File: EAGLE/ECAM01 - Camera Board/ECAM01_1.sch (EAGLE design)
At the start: 51 parts, among them J1 DCMI-PRELIM, J2 I2C1-2, J3 CPL-ETH-MAGJACK-PULSE, J4 USART1, J5 USART2, J6 CPL-CON-USB-B, Q1 TBD, Q2 25MHz, U1 32F429ZIT6U, U2 IS45S16400J, U3 CPL-ETH-PHY-LAN8720A, U4 74LVC1G04

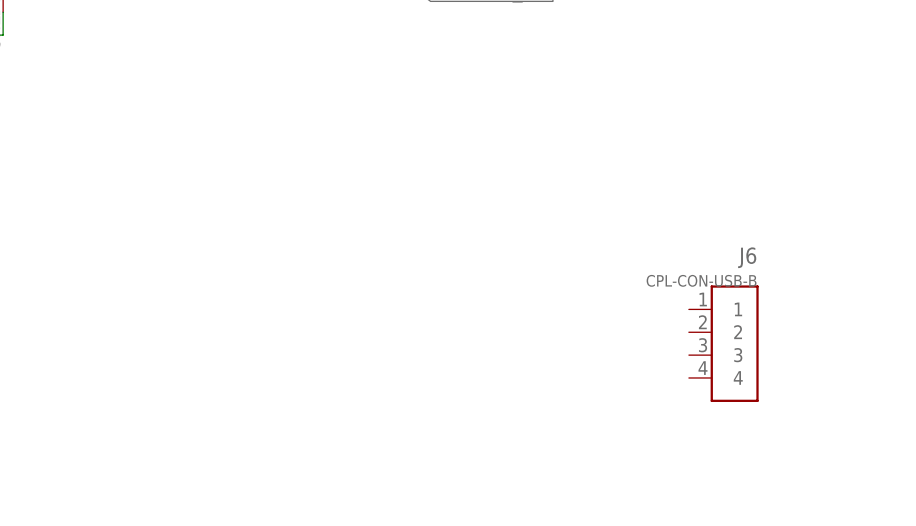
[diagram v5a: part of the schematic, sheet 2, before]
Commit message: Added USB connection to ECAM01 board, relevant devices.
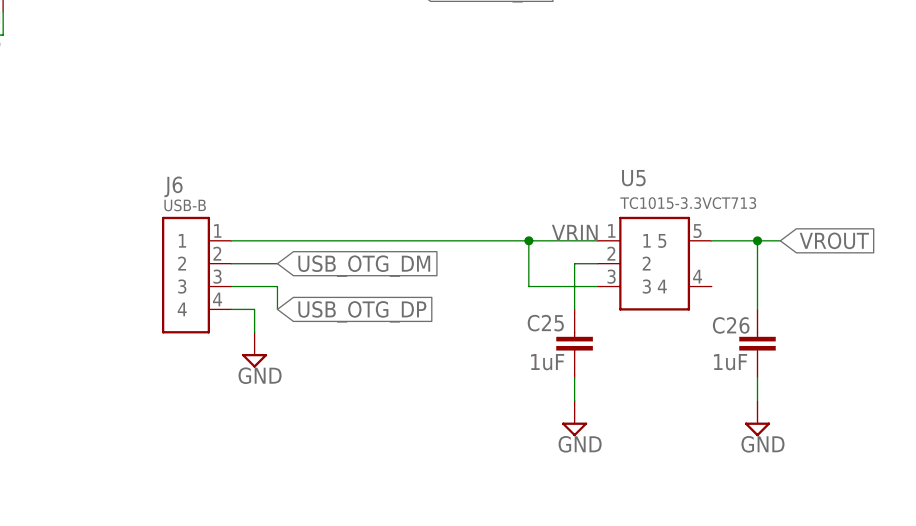
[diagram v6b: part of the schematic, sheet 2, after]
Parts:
- added C25, C26: 1uF, TinWhiskers:CPL-CAP-X5R-0603-1UF-50V
- added J7: CPL-CON-HEADER-0.1IN-3P-M, TinWhiskers:CPL-CON-HEADER-0.1IN-3P-M
- added U5: TC1015-3.3VCT713, TinWhiskers:CPL-REG-LIN-3.3V-0.1A
- J6: value CPL-CON-USB-B -> USB-B
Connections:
- removed net VDD: J1.10, J1.11, J1.4
- new net : J1.10, J1.11, J1.4, J7.2, U1.VDD@52
- new net N$17: C25.2, U5.2
- new net VRIN: J6.1, U5.1, U5.3
- new net VROUT: C26.2, J7.3, U5.5
- net GND: now also C25.1, C26.1, J6.4
- net USB_OTG_DM: now also J6.2
- net USB_OTG_DP: now also J6.3
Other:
- moved on the sheet: J6
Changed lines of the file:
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@@
 <setting verticaltext="up"/>
 </settings>
-<grid distance="0.1" unitdist="inch" unit="inch" style="lines" multiple="1" display="no" altdistance="0.01" altunitdist="inch" altunit="inch"/>
+<grid distance="0.1" unitdist="inch" unit="inch" style="lines" multiple="1" display="yes" altdistance="0.01" altunitdist="inch" altunit="inch"/>
 <layers>
 <layer number="1" name="Top" color="4" fill="1" visible="no" active="no"/>
@@
 <part name="J4" library="TinWhiskers" deviceset="CPL-CON-HEADER-0.1IN-2P-M" device="" value="USART1"/>
 <part name="J5" library="TinWhiskers" deviceset="CPL-CON-HEADER-0.1IN-4P-M" device="" value="USART2"/>
-<part name="J6" library="TinWhiskers" deviceset="CPL-CON-USB-B" device=""/>
+<part name="J6" library="TinWhiskers" deviceset="CPL-CON-USB-B" device="" value="USB-B"/>
+<part name="U5" library="TinWhiskers" deviceset="CPL-REG-LIN-3.3V-0.1A" device="" value="TC1015-3.3VCT713"/>
+<part name="SUPPLY6" library="TinWhiskers" deviceset="GND" device=""/>
+<part name="J7" library="TinWhiskers" deviceset="CPL-CON-HEADER-0.1IN-3P-M" device=""/>
+<part name="C25" library="TinWhiskers" deviceset="CPL-CAP-X5R-0603-1UF-50V" device="" value="1uF"/>
+<part name="C26" library="TinWhiskers" deviceset="CPL-CAP-X5R-0603-1UF-50V" device="" value="1uF"/>
+<part name="SUPPLY22" library="TinWhiskers" deviceset="GND" device=""/>
+<part name="SUPPLY23" library="TinWhiskers" deviceset="GND" device=""/>
 </parts>
 <sheets>
@@
 <instance part="DGND2" gate="1" x="330.2" y="76.2" smashed="yes">
 <attribute name="VALUE" x="327.66" y="73.66" size="1.778" layer="96"/>
+</instance>
+<instance part="J7" gate="G$1" x="193.04" y="243.84" smashed="yes" rot="R270">
+<attribute name="NAME" x="188.214" y="252.476" size="1.778" layer="95" font="vector" ratio="12"/>
 </instance>
 </instances>
@@
 </segment>
 </net>
-<net name="VDD" class="0">
+<net name="" class="0">
 <segment>
 <pinref part="J1" gate="G$1" pin="4"/>
@@
 <pinref part="J1" gate="G$1" pin="10"/>
 <pinref part="SUPPLY5" gate="VCC" pin="VCC"/>
+</segment>
+<segment>
+<pinref part="U1" gate="G$1" pin="VDD@52"/>
+<wire x1="193.04" y1="195.58" x2="193.04" y2="241.3" width="0.1524" layer="91"/>
+<pinref part="J7" gate="G$1" pin="2"/>
 </segment>
 </net>
@@
 <segment>
 <pinref part="U1" gate="G$1" pin="PB13"/>
-<wire x1="124.46" y1="114.3" x2="99.06" y2="114.3" width="0.1524" layer="91"/>
-<label x="99.06" y="114.3" size="1.778" layer="95" rot="R180" xref="yes"/>
+<wire x1="124.46" y1="114.3" x2="96.52" y2="114.3" width="0.1524" layer="91"/>
+<label x="96.52" y="114.3" size="1.778" layer="95" rot="R180" xref="yes"/>
 </segment>
 </net>
@@
 <segment>
 <pinref part="U1" gate="G$1" pin="PB15"/>
-<wire x1="124.46" y1="109.22" x2="99.06" y2="109.22" width="0.1524" layer="91"/>
-<label x="99.06" y="109.22" size="1.778" layer="95" rot="R180" xref="yes"/>
+<wire x1="124.46" y1="109.22" x2="96.52" y2="109.22" width="0.1524" layer="91"/>
+<label x="96.52" y="109.22" size="1.778" layer="95" rot="R180" xref="yes"/>
+</segment>
+</net>
+<net name="VROUT" class="0">
+<segment>
+<pinref part="J7" gate="G$1" pin="3"/>
+<wire x1="190.5" y1="241.3" x2="190.5" y2="238.76" width="0.1524" layer="91"/>
+<wire x1="190.5" y1="238.76" x2="187.96" y2="238.76" width="0.1524" layer="91"/>
+<label x="187.96" y="238.76" size="1.778" layer="95" rot="R180" xref="yes"/>
 </segment>
 </net>
@@
 <attribute name="VALUE" x="305.308" y="204.216" size="1.27" layer="96" font="vector" ratio="10"/>
 </instance>
-<instance part="J6" gate="G$1" x="355.6" y="149.86" rot="MR0"/>
+<instance part="J6" gate="G$1" x="299.72" y="157.48" smashed="yes">
+<attribute name="NAME" x="294.894" y="165.354" size="1.778" layer="95" font="vector" ratio="12"/>
+<attribute name="VALUE" x="294.64" y="163.322" size="1.27" layer="95" font="vector" ratio="10"/>
+</instance>
+<instance part="U5" gate="G$1" x="353.06" y="154.94" smashed="yes">
+<attribute name="NAME" x="345.44" y="166.116" size="1.778" layer="95" font="vector" ratio="12"/>
+<attribute name="VALUE" x="345.44" y="163.576" size="1.27" layer="95" font="vector" ratio="10"/>
+</instance>
+<instance part="SUPPLY6" gate="GND" x="304.8" y="147.32"/>
+<instance part="C25" gate="G$1" x="340.36" y="149.86" smashed="yes" rot="R90">
+<attribute name="NAME" x="335.026" y="149.987" size="1.778" layer="95"/>
+<attribute name="VALUE" x="335.28" y="145.669" size="1.778" layer="96"/>
+</instance>
+<instance part="C26" gate="G$1" x="360.68" y="149.86" smashed="yes" rot="R90">
+<attribute name="NAME" x="355.6" y="149.733" size="1.778" layer="95"/>
+<attribute name="VALUE" x="355.6" y="145.669" size="1.778" layer="96"/>
+</instance>
+<instance part="SUPPLY22" gate="GND" x="340.36" y="139.7"/>
+<instance part="SUPPLY23" gate="GND" x="360.68" y="139.7"/>
 </instances>
 <busses>
@@
 <junction x="271.78" y="182.88"/>
 <pinref part="SUPPLY21" gate="GND" pin="GND"/>
+</segment>
+<segment>
+<pinref part="J6" gate="G$1" pin="4"/>
+<wire x1="302.26" y1="152.4" x2="304.8" y2="152.4" width="0.1524" layer="91"/>
+<wire x1="304.8" y1="152.4" x2="304.8" y2="149.86" width="0.1524" layer="91"/>
+<pinref part="SUPPLY6" gate="GND" pin="GND"/>
+</segment>
+<segment>
+<pinref part="C25" gate="G$1" pin="1"/>
+<pinref part="SUPPLY22" gate="GND" pin="GND"/>
+<wire x1="340.36" y1="142.24" x2="340.36" y2="144.78" width="0.1524" layer="91"/>
+</segment>
+<segment>
+<pinref part="C26" gate="G$1" pin="1"/>
+<pinref part="SUPPLY23" gate="GND" pin="GND"/>
+<wire x1="360.68" y1="142.24" x2="360.68" y2="144.78" width="0.1524" layer="91"/>
 </segment>
 </net>
@@
 </segment>
 </net>
+<net name="VRIN" class="0">
+<segment>
+<pinref part="J6" gate="G$1" pin="1"/>
+<pinref part="U5" gate="G$1" pin="1"/>
+<wire x1="302.26" y1="160.02" x2="335.28" y2="160.02" width="0.1524" layer="91"/>
+<wire x1="335.28" y1="160.02" x2="342.9" y2="160.02" width="0.1524" layer="91"/>
+<wire x1="335.28" y1="160.02" x2="335.28" y2="154.94" width="0.1524" layer="91"/>
+<junction x="335.28" y="160.02"/>
+<pinref part="U5" gate="G$1" pin="3"/>
+<wire x1="335.28" y1="154.94" x2="342.9" y2="154.94" width="0.1524" layer="91"/>
+<label x="337.82" y="160.02" size="1.778" layer="95"/>
+</segment>
+</net>
+<net name="USB_OTG_DM" class="0">
+<segment>
+<pinref part="J6" gate="G$1" pin="2"/>
+<wire x1="302.26" y1="157.48" x2="307.34" y2="157.48" width="0.1524" layer="91"/>
+<label x="307.34" y="157.48" size="1.778" layer="95" xref="yes"/>
+</segment>
+</net>
+<net name="USB_OTG_DP" class="0">
+<segment>
+<pinref part="J6" gate="G$1" pin="3"/>
+<wire x1="302.26" y1="154.94" x2="307.34" y2="154.94" width="0.1524" layer="91"/>
+<wire x1="307.34" y1="154.94" x2="307.34" y2="152.4" width="0.1524" layer="91"/>
+<label x="307.34" y="152.4" size="1.778" layer="95" xref="yes"/>
+</segment>
+</net>
+<net name="N$17" class="0">
+<segment>
+<pinref part="U5" gate="G$1" pin="2"/>
+<wire x1="342.9" y1="157.48" x2="340.36" y2="157.48" width="0.1524" layer="91"/>
+<wire x1="340.36" y1="157.48" x2="340.36" y2="152.4" width="0.1524" layer="91"/>
+<pinref part="C25" gate="G$1" pin="2"/>
+</segment>
+</net>
+<net name="VROUT" class="0">
+<segment>
+<pinref part="U5" gate="G$1" pin="5"/>
+<wire x1="355.6" y1="160.02" x2="360.68" y2="160.02" width="0.1524" layer="91"/>
+<label x="363.22" y="160.02" size="1.778" layer="95" xref="yes"/>
+<wire x1="360.68" y1="160.02" x2="363.22" y2="160.02" width="0.1524" layer="91"/>
+<wire x1="360.68" y1="160.02" x2="360.68" y2="152.4" width="0.1524" layer="91"/>
+<junction x="360.68" y="160.02"/>
+<pinref part="C26" gate="G$1" pin="2"/>
+</segment>
+</net>

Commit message: Fixed error: line 13607: invalid value '' for attribute 'name' in tag <net>
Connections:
- net  renamed Dan
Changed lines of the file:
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@@
 </segment>
 </net>
-<net name="" class="0">
+<net name="Dan" class="0">
 <segment>
 <pinref part="J1" gate="G$1" pin="4"/>

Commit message: Created parts for EMC03, began schematic for EMC03. Symbol for NXP microchip in preliminary format.
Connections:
- net Dan renamed VDD
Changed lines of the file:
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@@
 <setting verticaltext="up"/>
 </settings>
-<grid distance="0.1" unitdist="inch" unit="inch" style="lines" multiple="1" display="yes" altdistance="0.01" altunitdist="inch" altunit="inch"/>
+<grid distance="0.1" unitdist="inch" unit="inch" style="lines" multiple="1" display="no" altdistance="0.01" altunitdist="inch" altunit="inch"/>
 <layers>
 <layer number="1" name="Top" color="4" fill="1" visible="no" active="no"/>
@@
 </segment>
 </net>
-<net name="Dan" class="0">
+<net name="VDD" class="0">
 <segment>
 <pinref part="J1" gate="G$1" pin="4"/>
